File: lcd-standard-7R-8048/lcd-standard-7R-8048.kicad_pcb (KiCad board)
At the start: 2 copper layers, 181 x 108.2 mm, 114 parts, among them J1 SWD, J10 Conn_01x10_MountingPin, J2 Conn_01x40_MountingPin, J3 Micro_SD_Card_Det1, J4 USB_C_Receptacle_USB2.0_16P, J6 Serial, J7 Conn_ARM_JTAG_SWD_10, J8 Conn_01x02_MountingPin, J9 Conn_01x10_MountingPin, Q1 DMG2301L, Q2 MMBT3904, Q3 MMBT3904, Q4 MMBT3904, SW1 BOOT0, SW2 RST, U1 MAX98357A, U2 TPS61169, U3 XPT2046TS, U4 CAT24C256, U5 AMS1117-3.3, U6 siplex-som-s16

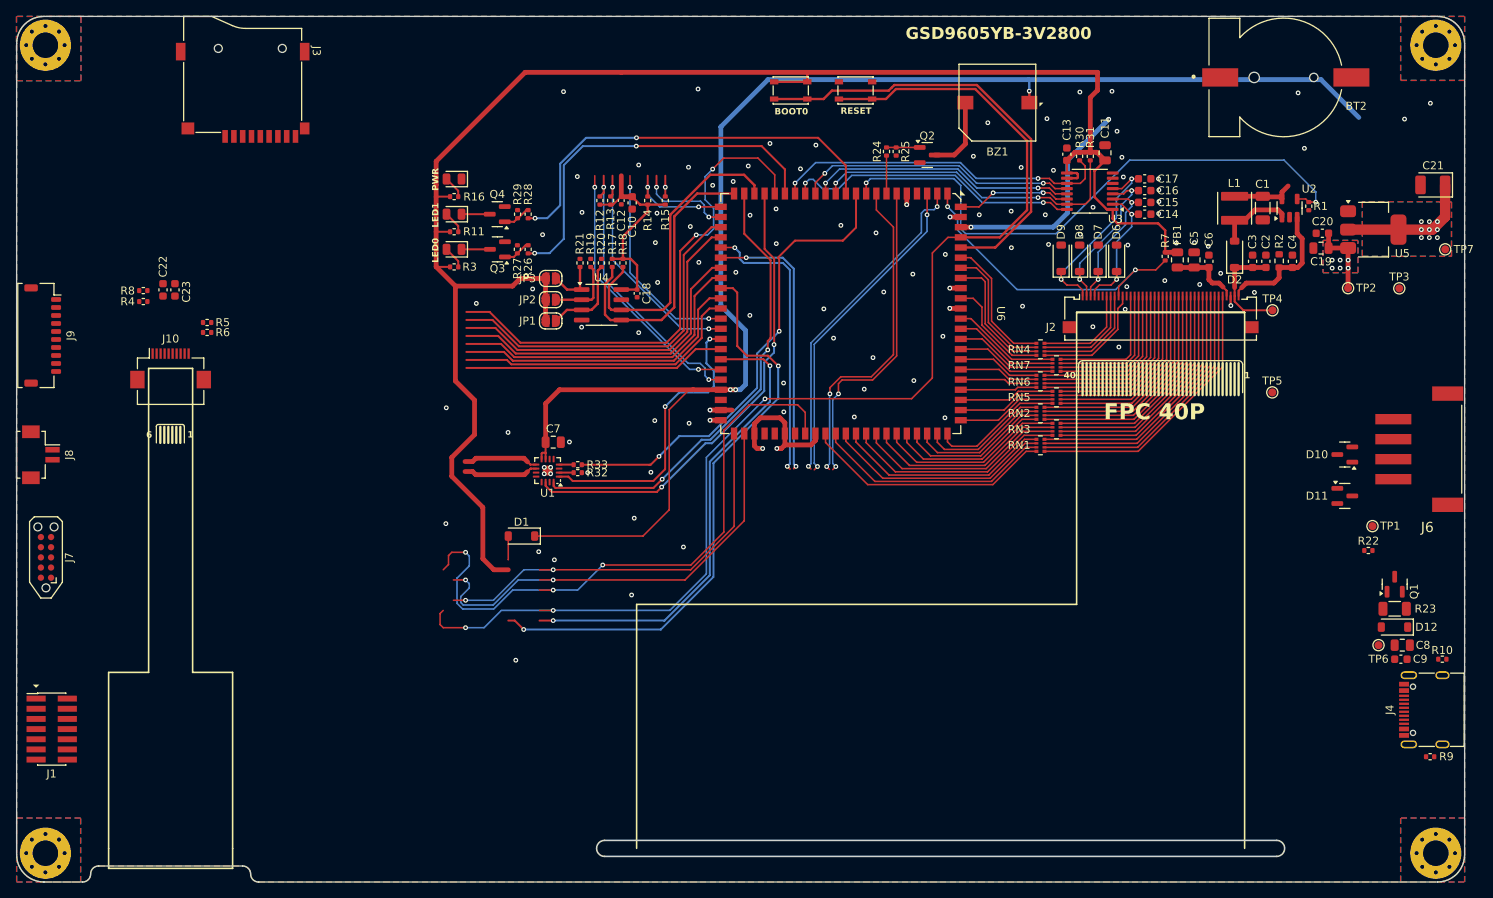
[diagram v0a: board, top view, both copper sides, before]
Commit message: Layouting LCD 7R, LED's and PWR tracks left
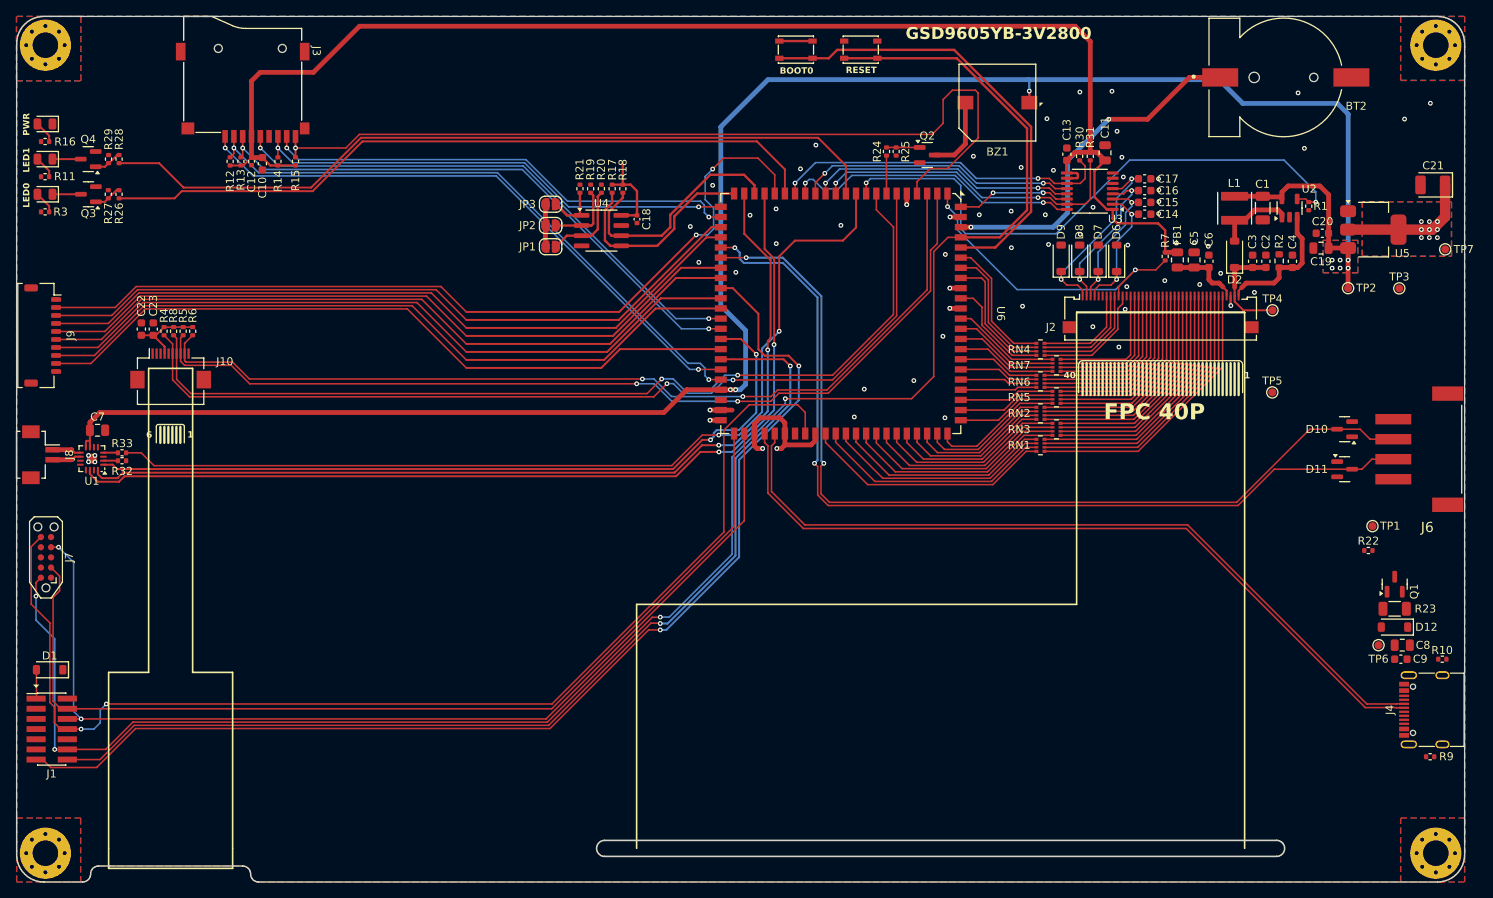
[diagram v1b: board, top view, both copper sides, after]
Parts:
- moved D1 61.3 mm to (30.3, 130.7)
- moved R32 57.0 mm to (39.3, 104.6)
- moved R33 57.0 mm to (39.3, 103.6)
- moved C7 57.0 mm to (36.2, 100.7)
- moved U1 57.0 mm to (35.5, 104.3)
- moved R11 51.6 mm to (29.7, 69.0)
- moved R16 51.6 mm to (29.7, 64.7)
- moved R3 51.6 mm to (29.7, 73.4)
- moved R29 51.6 mm to (37.6, 66.9)
- moved D4 51.6 mm to (29.7, 66.9)
- moved D5 51.6 mm to (29.7, 62.5)
- moved Q4 51.6 mm to (35.1, 66.9)
- moved R28 51.6 mm to (38.9, 66.9)
- moved Q3 51.6 mm to (35.1, 71.2)
- moved R27 51.6 mm to (37.6, 71.2)
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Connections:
- J10 pad 1: GND -> unconnected-(J10-Pin_1-Pad1)
- J10 pad 10: unconnected-(J10-Pin_10-Pad10) -> GND
- J10 pad 2: /TP_SDA -> unconnected-(J10-Pin_2-Pad2)
- J10 pad 3: /TP_SCL -> unconnected-(J10-Pin_3-Pad3)
- J10 pad 4: /TP_WAKE -> +3V3
- J10 pad 5: /TP_INT -> unconnected-(J10-Pin_5-Pad5)
- J10 pad 6: unconnected-(J10-Pin_6-Pad6) -> /TP_INT
- J10 pad 7: +3V3 -> /TP_WAKE
- J10 pad 8: unconnected-(J10-Pin_8-Pad8) -> /TP_SCL
- J10 pad 9: unconnected-(J10-Pin_9-Pad9) -> /TP_SDA
- U6 pad 4: unconnected-(U6-PH4-Pad4) -> /SD_DET
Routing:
- net /SD_DET: track 2.59 -> 109.8 mm
- net /USB_DN: track 0.00 -> 98.2 mm
- net /USB_DP: track 0.00 -> 97.5 mm
- net /SERIAL_RX: track 34.9 -> 115.8 mm
- net /SERIAL_TX: track 35.4 -> 115.1 mm
- net /TP_INT: track 40.4 -> 117.9 mm
- net /TP_WAKE: track 41.2 -> 117.3 mm
- net /TP_SCL: track 41.9 -> 117.4 mm
- net /TP_SDA: track 40.7 -> 115.8 mm
- net /RESET: track 151.8 -> 225.5 mm, vias 3 -> 4
- net /SWCLK: track 57.5 -> 129.3 mm
- net /SWDIO: track 52.2 -> 124.0 mm, vias 2 -> 0
- net /DBG_TX: track 59.4 -> 129.7 mm
- net /SWO: track 78.2 -> 147.3 mm, vias 3 -> 2
- net /DBG_RX: track 73.7 -> 142.8 mm
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
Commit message: Added sd_det tracks
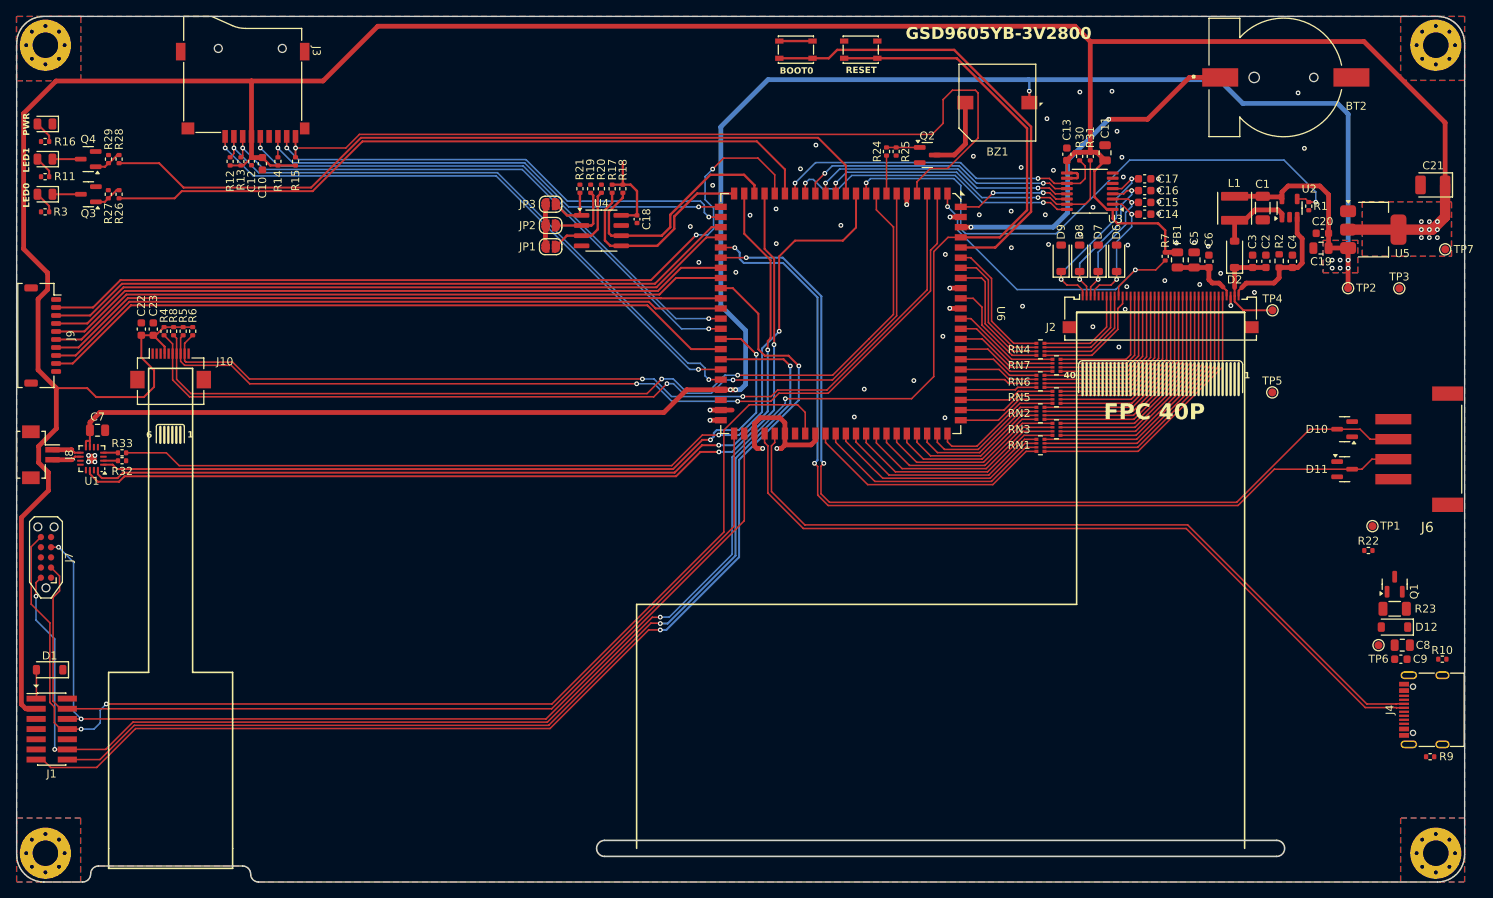
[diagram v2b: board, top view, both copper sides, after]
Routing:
- net +3V3: track 219.4 -> 407.6 mm
- net /IO_2: track 90.8 -> 85.7 mm
- net /IO_1: track 91.1 -> 86.2 mm
- net /IO_3: track 90.9 -> 86.3 mm
- net /IO_4: track 90.5 -> 86.4 mm
- net /IO_5: track 91.2 -> 87.5 mm
- net /IO_6: track 90.8 -> 87.7 mm
- net /IO_7: track 108.7 -> 106.1 mm
- net /IO_0: track 89.9 -> 88.4 mm
- net GND: vias 65 -> 63
